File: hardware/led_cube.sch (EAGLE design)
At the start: 81 parts, among them IC1 74LS164N, IC2 74LS164N, IC3 74LS164N, IC4 74LS164N, T1 2N2222, T2 2N2222, T3 2N2222, T4 2N2222, U1 ARDUINO_SHIELDNO_SILK

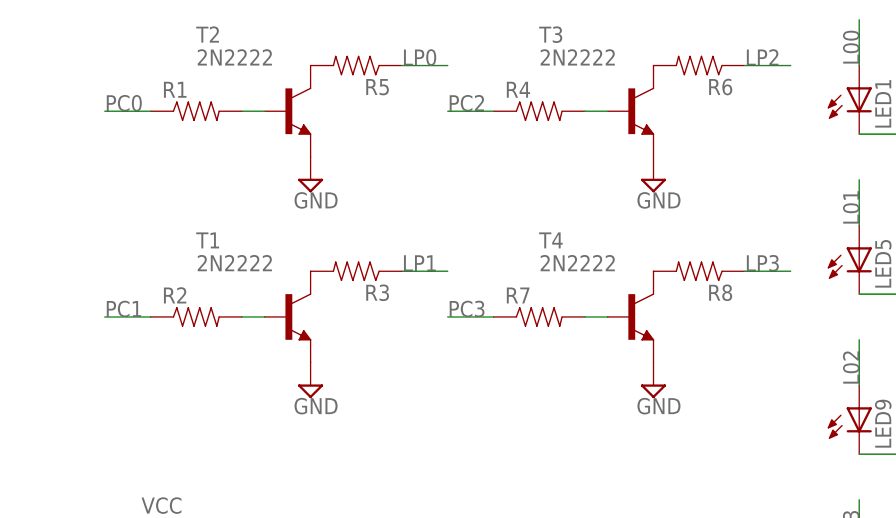
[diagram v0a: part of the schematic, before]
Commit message: added resistor values to schematic
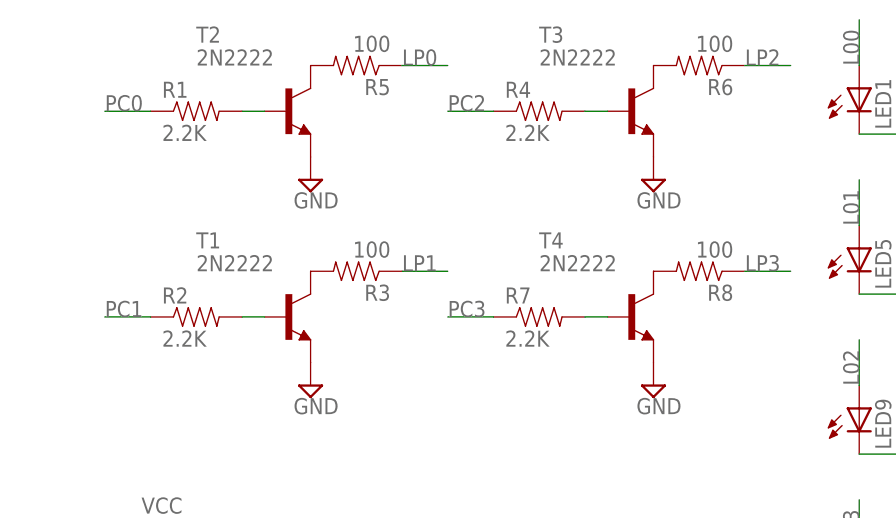
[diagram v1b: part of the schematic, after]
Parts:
- R1, R2, R4, R7: value (none) -> 2.2K
- R3, R5, R6, R8: value (none) -> 100
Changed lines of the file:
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@@
 <part name="P+2" library="SparkFun" deviceset="VCC" device=""/>
 <part name="T2" library="adafruit" deviceset="2N2222" device=""/>
-<part name="R1" library="SparkFun" deviceset="RESISTOR" device="0603-RES"/>
+<part name="R1" library="SparkFun" deviceset="RESISTOR" device="0603-RES" value="2.2K"/>
 <part name="SUPPLY2" library="supply2" deviceset="GND" device=""/>
-<part name="R5" library="SparkFun" deviceset="RESISTOR" device="0603-RES"/>
+<part name="R5" library="SparkFun" deviceset="RESISTOR" device="0603-RES" value="100"/>
 <part name="T1" library="adafruit" deviceset="2N2222" device=""/>
-<part name="R2" library="SparkFun" deviceset="RESISTOR" device="0603-RES"/>
+<part name="R2" library="SparkFun" deviceset="RESISTOR" device="0603-RES" value="2.2K"/>
 <part name="SUPPLY3" library="supply2" deviceset="GND" device=""/>
-<part name="R3" library="SparkFun" deviceset="RESISTOR" device="0603-RES"/>
+<part name="R3" library="SparkFun" deviceset="RESISTOR" device="0603-RES" value="100"/>
 <part name="T3" library="adafruit" deviceset="2N2222" device=""/>
-<part name="R4" library="SparkFun" deviceset="RESISTOR" device="0603-RES"/>
+<part name="R4" library="SparkFun" deviceset="RESISTOR" device="0603-RES" value="2.2K"/>
 <part name="SUPPLY4" library="supply2" deviceset="GND" device=""/>
-<part name="R6" library="SparkFun" deviceset="RESISTOR" device="0603-RES"/>
+<part name="R6" library="SparkFun" deviceset="RESISTOR" device="0603-RES" value="100"/>
 <part name="T4" library="adafruit" deviceset="2N2222" device=""/>
-<part name="R7" library="SparkFun" deviceset="RESISTOR" device="0603-RES"/>
+<part name="R7" library="SparkFun" deviceset="RESISTOR" device="0603-RES" value="2.2K"/>
 <part name="SUPPLY5" library="supply2" deviceset="GND" device=""/>
-<part name="R8" library="SparkFun" deviceset="RESISTOR" device="0603-RES"/>
+<part name="R8" library="SparkFun" deviceset="RESISTOR" device="0603-RES" value="100"/>
 <part name="LED1" library="led" deviceset="LED" device=""/>
 <part name="LED2" library="led" deviceset="LED" device=""/>
